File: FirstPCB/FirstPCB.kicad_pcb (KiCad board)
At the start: 2 copper layers, 8 parts, among them J1 Output, J2 Output, J3 Bias Connector, U1 AD711

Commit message: rough PCB optimised
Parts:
- C1: footprint Capacitor_THT:C_Radial_D5.0mm_H5.0mm_P2.00mm -> Capacitor_THT:C_Rect_L7.0mm_W2.5mm_P5.00mm
- C2: footprint Capacitor_THT:C_Radial_D5.0mm_H5.0mm_P2.00mm -> Capacitor_THT:C_Rect_L7.0mm_W2.0mm_P5.00mm
- U1: footprint FirstPCB:AD711_PDIP -> Package_DIP:DIP-8_W7.62mm_LongPads
- moved U1 5.39 mm to (114.8, 72.6), turned to 90 degrees
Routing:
- net VSS: track 23.5 -> 30.4 mm
- net VCC: track 49.8 -> 44.8 mm

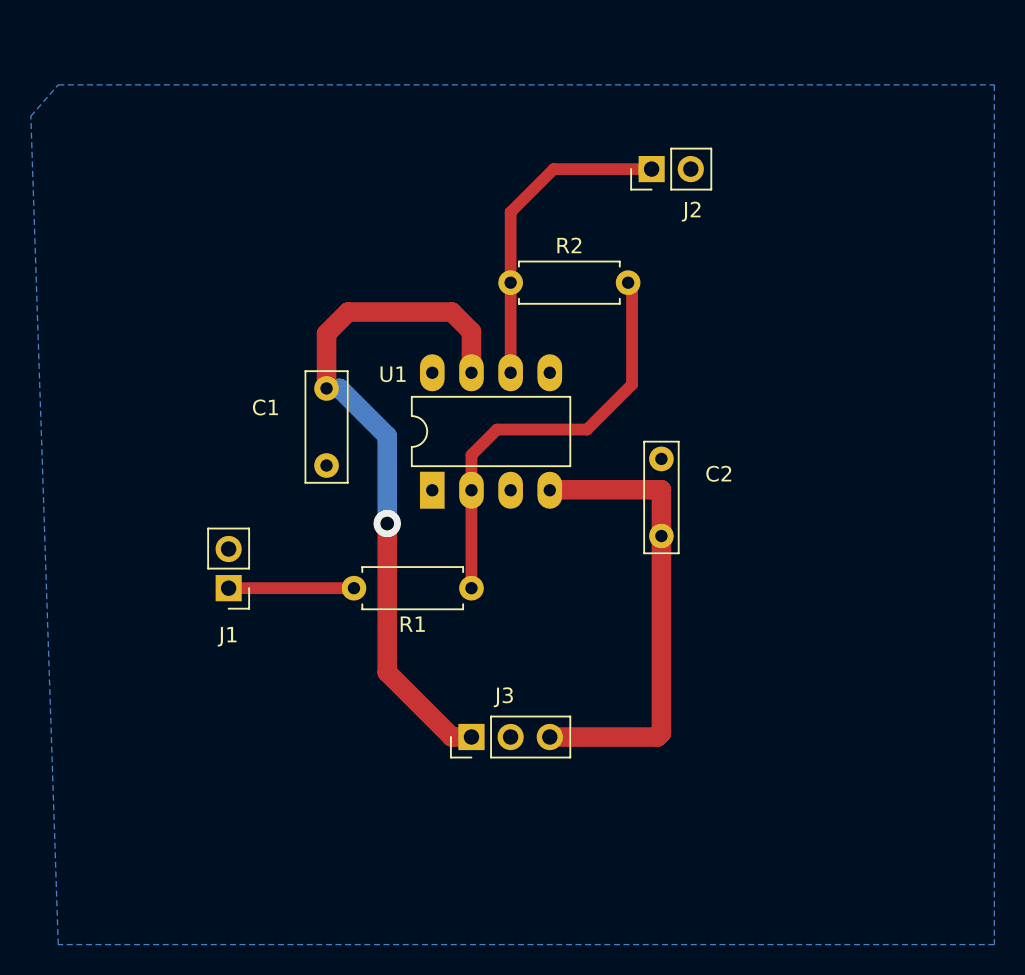
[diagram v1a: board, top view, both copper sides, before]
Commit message: First PCB done with margin and mouting screws
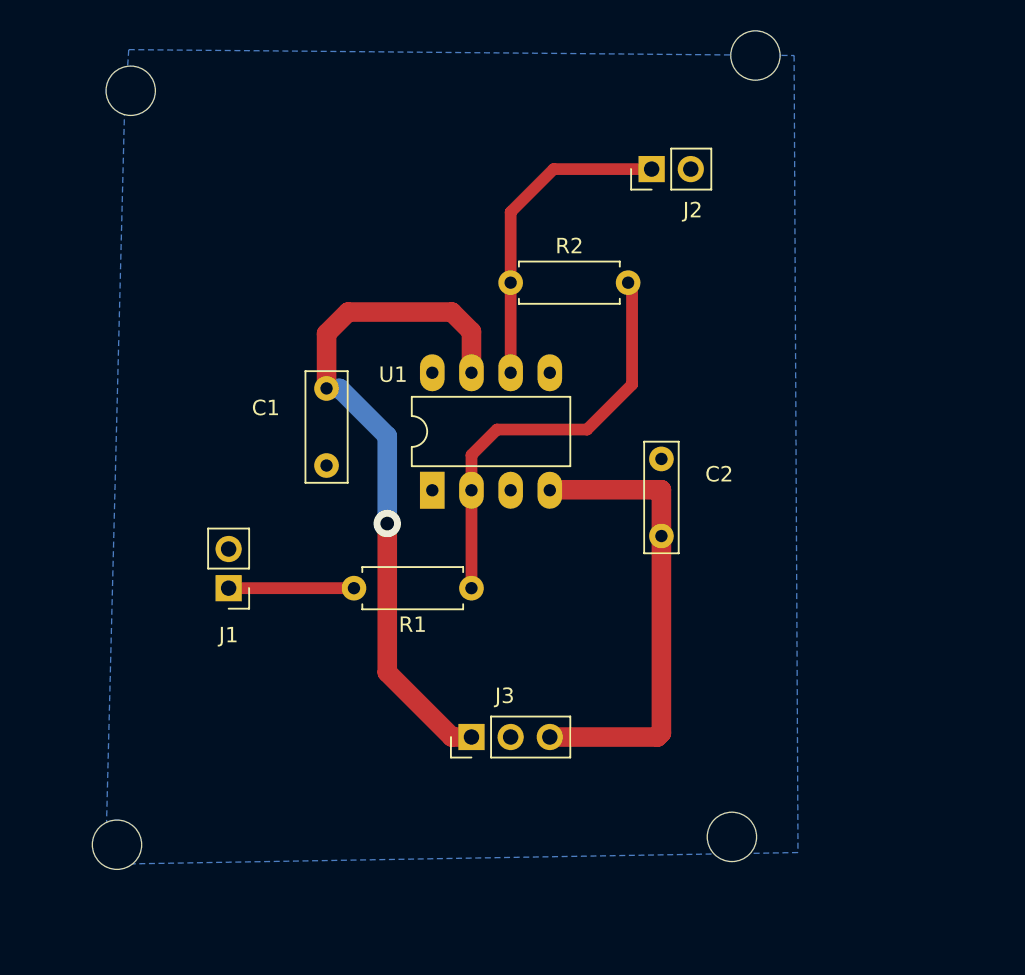
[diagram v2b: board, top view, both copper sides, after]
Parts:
- added REF**: m3, MountingHole:MountingHole_3.2mm_M3, F.Cu at (134.2, 95.1)
- added REF**: m3, MountingHole:MountingHole_3.2mm_M3, F.Cu at (94.4, 95.6)
- added REF**: MountingHole_3.2mm_M3, MountingHole:MountingHole_3.2mm_M3, F.Cu at (135.8, 44.5)
- added REF**: MountingHole_3.2mm_M3, MountingHole:MountingHole_3.2mm_M3, F.Cu at (95.2, 46.7)
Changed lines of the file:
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@@
   (general
     (thickness 1.6)
-    (drawings 0)
+    (drawings 5)
     (tracks 31)
     (zones 0)
-    (modules 8)
+    (modules 12)
     (nets 10)
   )
@@
     (add_net VSS)
   )
+  (module MountingHole:MountingHole_3.2mm_M3 (layer F.Cu)
+    (at 134.239 95.123)
+    (descr "Mounting Hole 3.2mm, no annular, M3")
+    (tags "mounting hole 3.2mm no annular m3")
+    (attr virtual)
+    (fp_text reference REF** (at 0 -4.2) (layer F.SilkS) hide
+      (effects (font (size 1 1) (thickness 0.15)))
+    )
+    (fp_text value m3 (at 0 4.2) (layer F.Fab)
+      (effects (font (size 1 1) (thickness 0.15)))
+    )
+    (fp_circle (center 0 0) (end 3.2 0) (layer Cmts.User) (width 0.15))
+    (fp_circle (center 0 0) (end 3.45 0) (layer F.CrtYd) (width 0.05))
+    (fp_text user %R (at 6.096 -1.778) (layer F.Fab)
+      (effects (font (size 1 1) (thickness 0.15)))
+    )
+    (pad 1 np_thru_hole circle (at 0 0) (size 3.2 3.2) (drill 3.2) (layers *.Cu *.Mask))
+  )
+  (module MountingHole:MountingHole_3.2mm_M3 (layer F.Cu)
+    (at 94.361 95.631)
+    (descr "Mounting Hole 3.2mm, no annular, M3")
+    (tags "mounting hole 3.2mm no annular m3")
+    (attr virtual)
+    (fp_text reference REF** (at 0 -4.2) (layer F.SilkS) hide
+      (effects (font (size 1 1) (thickness 0.15)))
+    )
+    (fp_text value m3 (at 0 4.2) (layer F.Fab)
+      (effects (font (size 1 1) (thickness 0.15)))
+    )
+    (fp_circle (center 0 0) (end 3.2 0) (layer Cmts.User) (width 0.15))
+    (fp_circle (center 0 0) (end 3.45 0) (layer F.CrtYd) (width 0.05))
+    (fp_text user %R (at 6.096 -1.778) (layer F.Fab)
+      (effects (font (size 1 1) (thickness 0.15)))
+    )
+    (pad 1 np_thru_hole circle (at 0 0) (size 3.2 3.2) (drill 3.2) (layers *.Cu *.Mask))
+  )
+  (module MountingHole:MountingHole_3.2mm_M3 (layer F.Cu)
+    (at 135.763 44.45)
+    (descr "Mounting Hole 3.2mm, no annular, M3")
+    (tags "mounting hole 3.2mm no annular m3")
+    (attr virtual)
+    (fp_text reference REF** (at 0 -4.2) (layer F.SilkS) hide
+      (effects (font (size 1 1) (thickness 0.15)))
+    )
+    (fp_text value MountingHole_3.2mm_M3 (at -13.843 -3.683) (layer F.Fab)
+      (effects (font (size 1 1) (thickness 0.15)))
+    )
+    (fp_text user %R (at 0.3 0) (layer F.Fab)
+      (effects (font (size 1 1) (thickness 0.15)))
+    )
+    (fp_circle (center 0 0) (end 3.2 0) (layer Cmts.User) (width 0.15))
+    (fp_circle (center 0 0) (end 3.45 0) (layer F.CrtYd) (width 0.05))
+    (pad 1 np_thru_hole circle (at 0 0) (size 3.2 3.2) (drill 3.2) (layers *.Cu *.Mask))
+  )
+  (module MountingHole:MountingHole_3.2mm_M3 (layer F.Cu)
+    (at 95.25 46.736)
+    (descr "Mounting Hole 3.2mm, no annular, M3")
+    (tags "mounting hole 3.2mm no annular m3")
+    (attr virtual)
+    (fp_text reference REF** (at 0 -4.2) (layer F.SilkS) hide
+      (effects (font (size 1 1) (thickness 0.15)))
+    )
+    (fp_text value MountingHole_3.2mm_M3 (at 0 4.2) (layer F.Fab)
+      (effects (font (size 1 1) (thickness 0.15)))
+    )
+    (fp_text user %R (at 6.096 -1.778) (layer F.Fab)
+      (effects (font (size 1 1) (thickness 0.15)))
+    )
+    (fp_circle (center 0 0) (end 3.2 0) (layer Cmts.User) (width 0.15))
+    (fp_circle (center 0 0) (end 3.45 0) (layer F.CrtYd) (width 0.05))
+    (pad 1 np_thru_hole circle (at 0 0) (size 3.2 3.2) (drill 3.2) (layers *.Cu *.Mask))
+  )
   (module Package_DIP:DIP-8_W7.62mm_LongPads (layer F.Cu)
     (at 114.808 72.644 90)
@@
     )
   )
+  (gr_line (start 141.351 102.235) (end 89.027 102.235) (layer Margin) (width 0.15))
+  (gr_line (start 89.027 102.235) (end 89.027 102.108) (layer Margin) (width 0.15))
+  (gr_line (start 89.027 38.227) (end 89.027 102.108) (layer Margin) (width 0.15))
+  (gr_line (start 141.351 38.227) (end 89.027 38.227) (layer Margin) (width 0.15))
+  (gr_line (start 141.351 102.235) (end 141.351 38.227) (layer Margin) (width 0.15))
   (segment (start 117.094 64.77) (end 117.348 65.024) (width 0.762) (layer F.Cu) (net 2))
   (segment (start 117.348 88.646) (end 116.078 88.646) (width 1.27) (layer F.Cu) (net 2))
@@
     (polygon
       (pts
-        (xy 151.257 102.108) (xy 90.551 102.108) (xy 88.773 48.387) (xy 90.551 46.355) (xy 151.257 46.355)
+        (xy 138.52525 96.139) (xy 93.614875 96.901) (xy 94.845188 48.1965) (xy 95.123 44.069) (xy 138.27125 44.45)
       )
     )
